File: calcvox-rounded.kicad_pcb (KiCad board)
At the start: 2 copper layers, 165.1 x 219.7 mm, 148 parts, among them J1 AudioJack2_Ground_Switch, SW1 RotaryEncoder_Switch, SW10 SW_Push, SW11 SW_Push, SW12 SW_Push, SW13 SW_Push, SW14 SW_Push, SW15 SW_Push, SW16 SW_Push, SW17 SW_Push, SW18 SW_Push, SW19 SW_Push, SW2 SW_Push, SW20 SW_Push, SW21 SW_Push, SW22 SW_Push, SW23 SW_Push, SW24 SW_Push, SW25 SW_Push, SW26 SW_Push, SW27 SW_Push, SW28 SW_Push, SW29 SW_Push, SW3 SW_Push, SW30 SW_Push, SW31 SW_Push, SW32 SW_Push, SW33 SW_Push, SW34 SW_Push, SW35 SW_Push, SW36 SW_Push, SW37 SW_Push, SW38 SW_Push, SW39 SW_Push, SW4 SW_Push, SW40 SW_Push, SW41 SW_Push, SW42 SW_Push, SW43 SW_Push, SW44 SW_Push, SW45 SW_Push, SW46 SW_Push, SW47 SW_Push, SW48 SW_Push, SW49 SW_Push, SW5 SW_Push, SW50 SW_Push, SW51 SW_Push, SW52 SW_Push, SW53 SW_Push, SW54 SW_Push, SW55 SW_Push, SW56 SW_Push, SW57 SW_Push, SW58 SW_Push, SW59 SW_Push, SW6 SW_Push, SW60 SW_Push, SW61 SW_Push, SW62 SW_Push, SW63 SW_Push, SW64 SW_Push, SW65 SW_Push, SW66 SW_Push, SW67 SW_SPDT, SW7 SW_Push, SW8 SW_Push, SW9 SW_Push

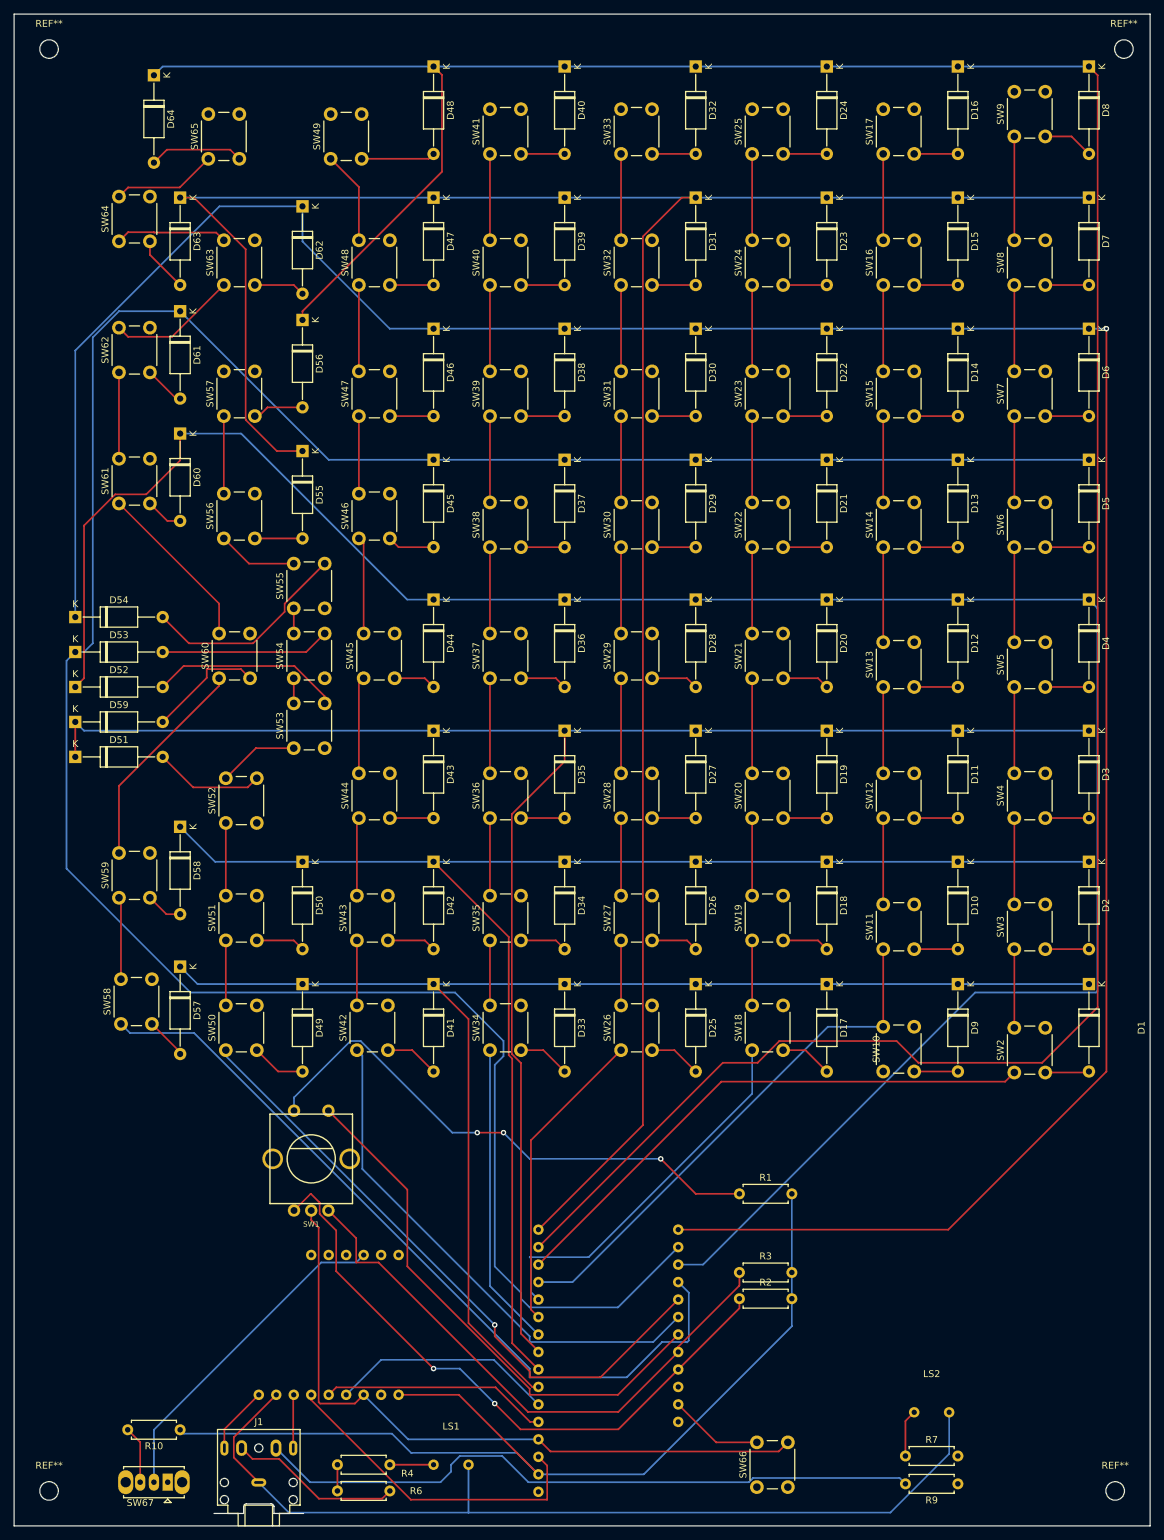
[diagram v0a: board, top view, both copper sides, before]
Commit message: updated schematics
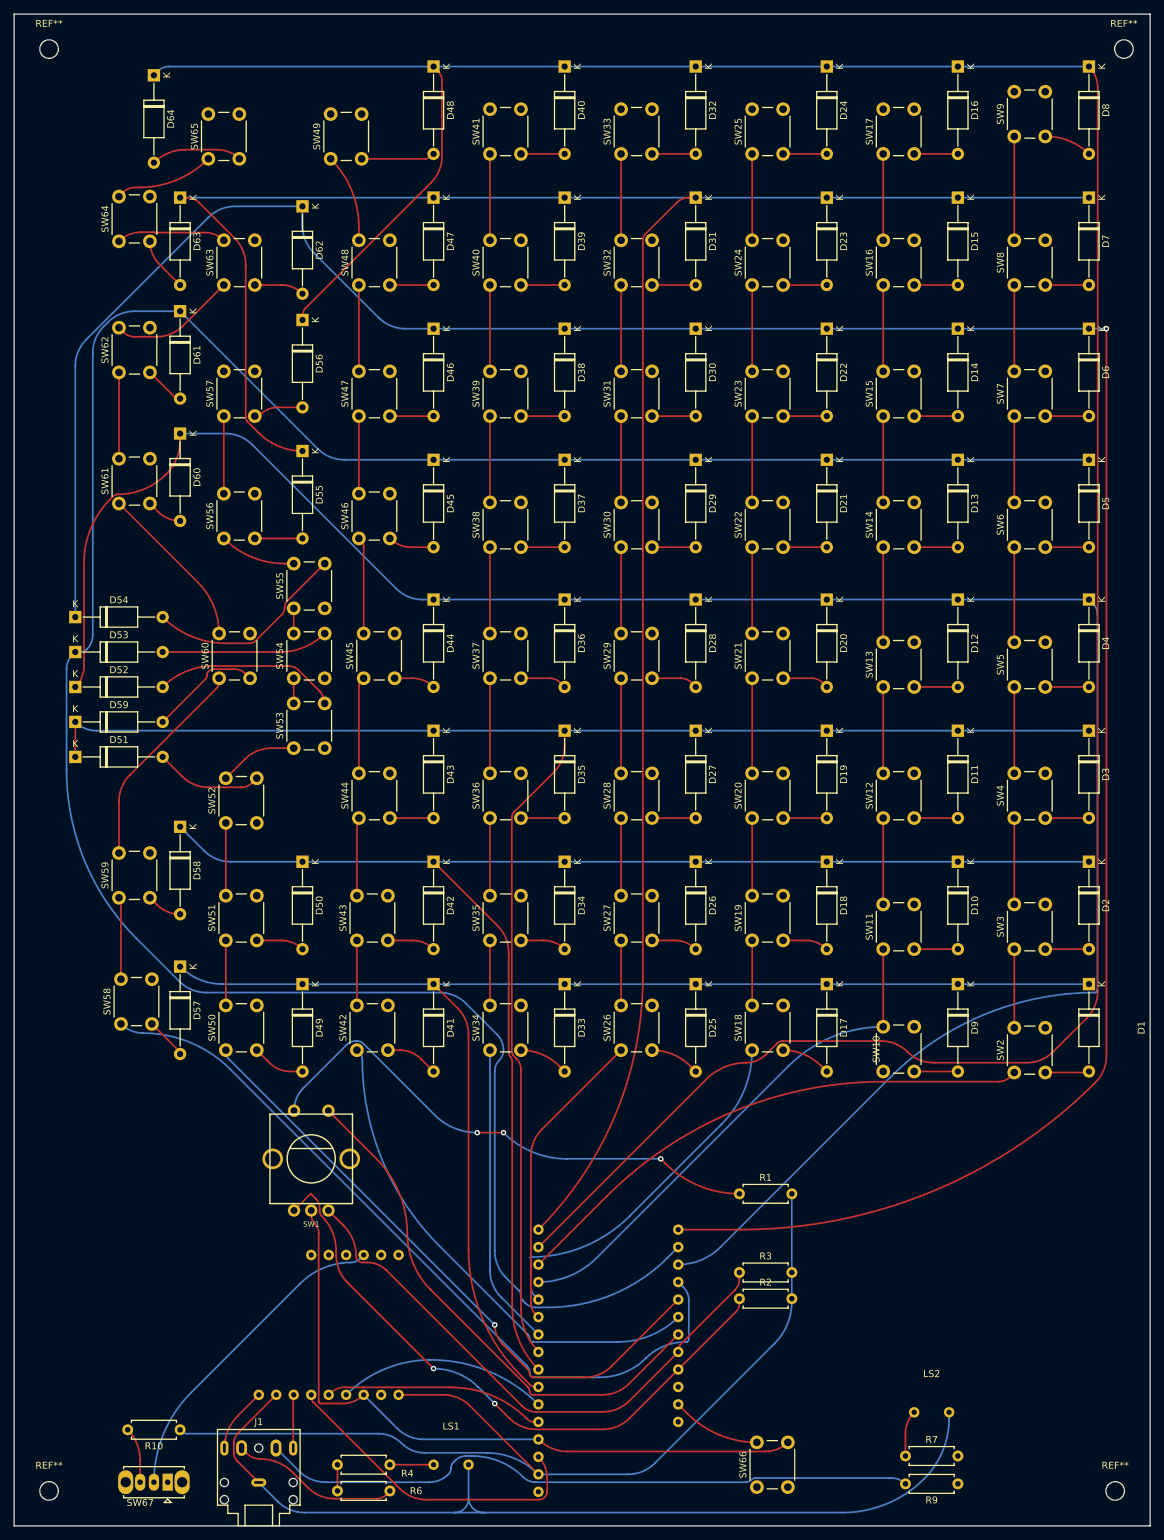
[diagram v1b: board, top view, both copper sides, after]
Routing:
- net R5: track 375.3 -> 369.9 mm
- net C8: track 247.9 -> 242.7 mm
- net R6: track 387.3 -> 382.5 mm
- net R4: track 322.6 -> 317.9 mm
- net C6: track 162.3 -> 158.8 mm
- net R7: track 340.3 -> 336.8 mm
- net C1: track 171.3 -> 168.4 mm
- net Net-(J1-PadG): track 135.5 -> 138.0 mm
- net R8: track 417.7 -> 415.3 mm
- net Net-(R1-Pad1): track 79.3 -> 77.1 mm
- net R1: track 198.5 -> 196.5 mm
- net C3: track 139.9 -> 138.0 mm
- net Net-(R1-Pad2): track 144.8 -> 142.9 mm
- net Net-(UDA1334Breakout1-PadWSEL): track 32.7 -> 30.8 mm
- net Net-(SW1-PadS2): track 78.6 -> 76.8 mm
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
